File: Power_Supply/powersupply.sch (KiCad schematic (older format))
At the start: 80 parts, among them J1 1x2, J101 USB_B_Micro, J102 Conn_01x03_Male, J103 Default_Jumper, J104 Default_Jumper, J2 1x2, Q1 IRF9Z24NPBF, SW1 KMR2, SW2 joystick-K1-1506DN-01, U101 AZ1117E-3.3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

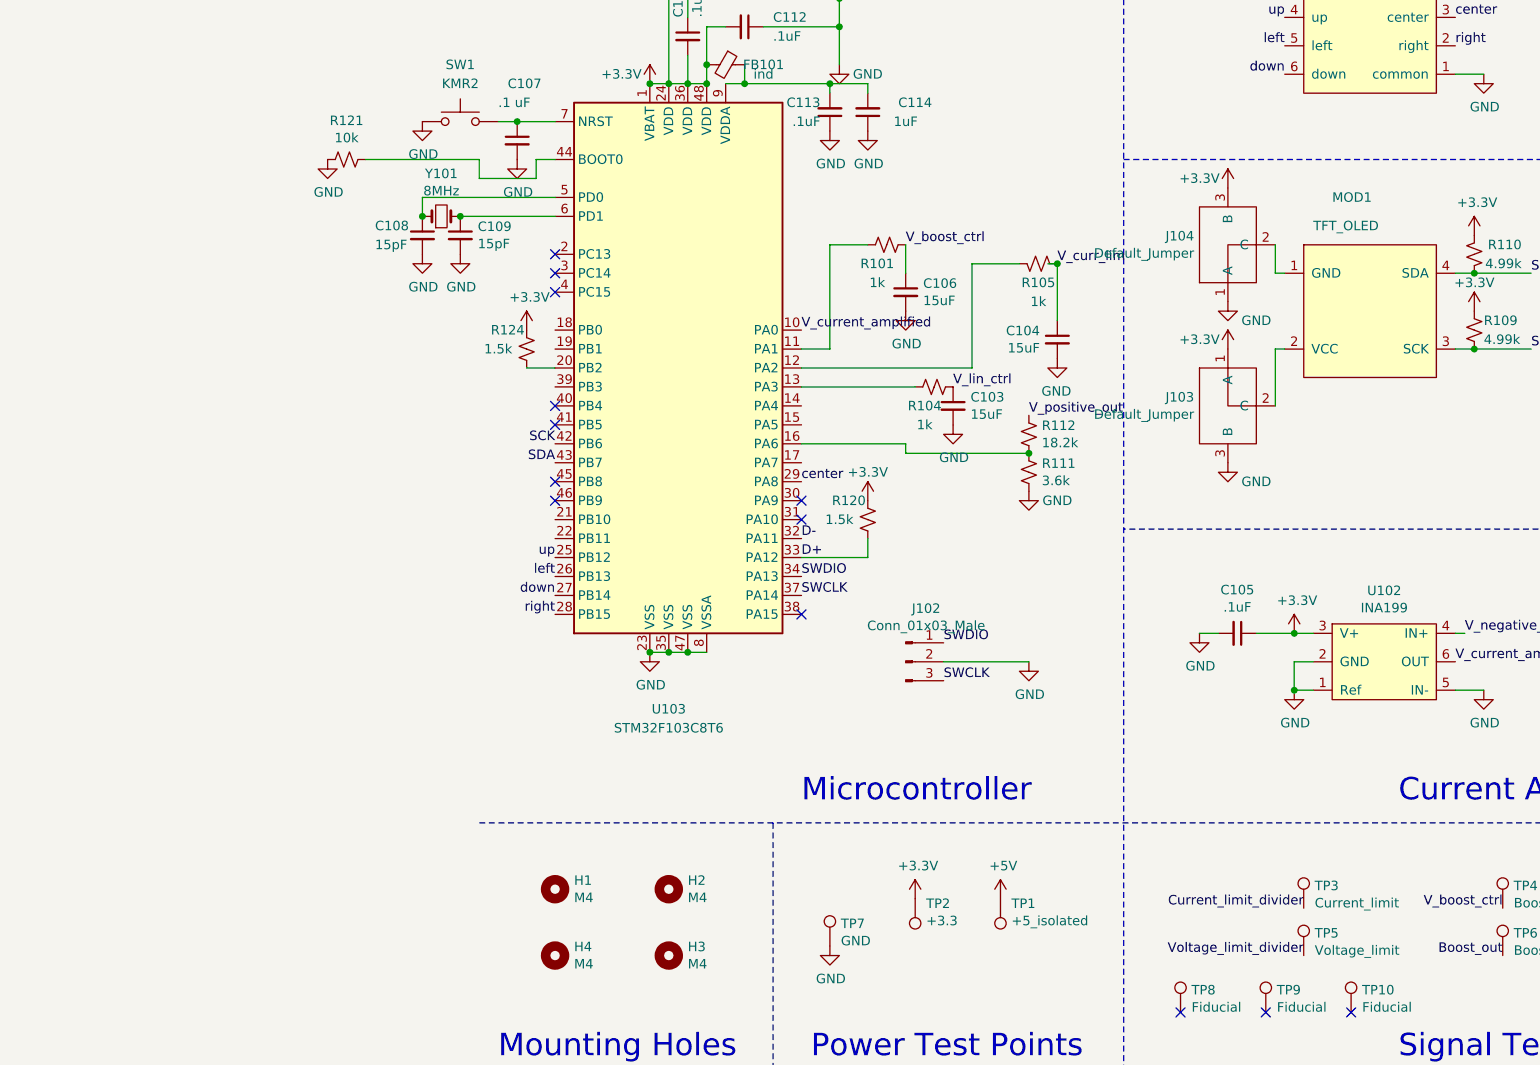
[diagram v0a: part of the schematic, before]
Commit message: Stuff for bootloader and MOSFET flat orientation
Moved power stuff to left and changed mosfet to flat orientation
Added LED for bootloader
Added button for entering bootloader mode
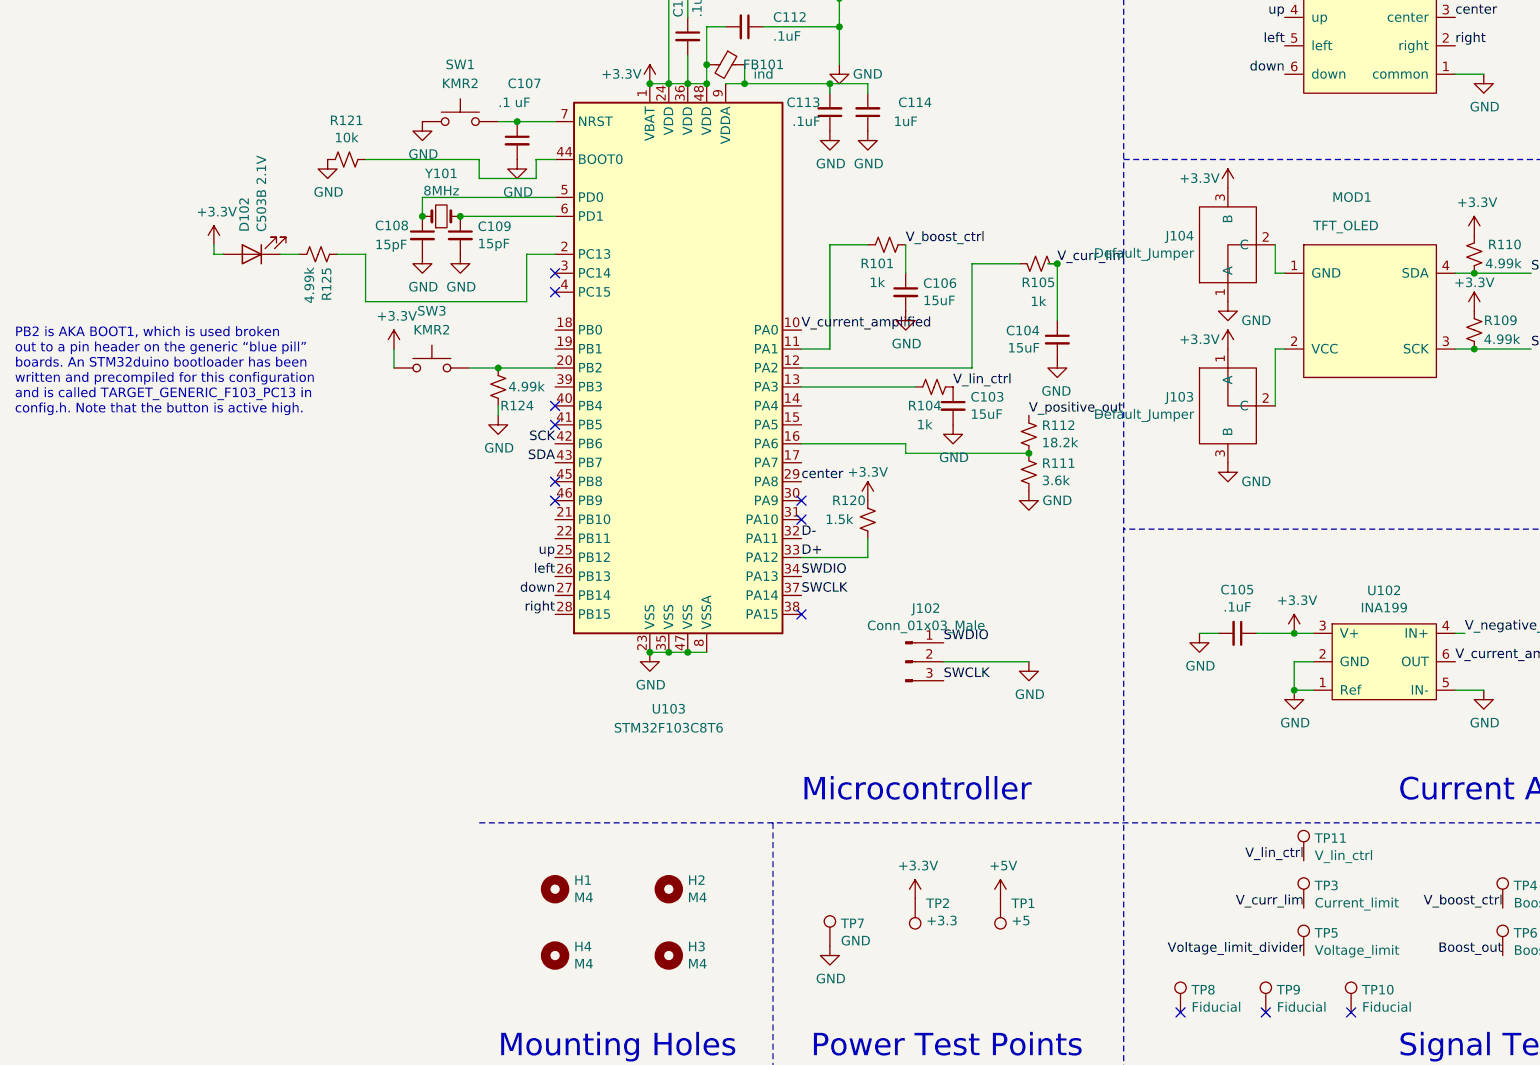
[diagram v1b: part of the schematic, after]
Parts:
- added D102: C503B 2.1V, LED_SMD:LED_0805_2012Metric, symbol Device:LED
- added R125: 4.99k, Resistor_SMD:R_0805_2012Metric, symbol Device:R_Small_US
- added SW3: KMR2, Button_Switch_SMD:SW_Push_1P1T_NO_CK_KMR2, symbol Switch:SW_Push
- added TP11: V_lin_ctrl, TestPoint:TestPoint_THTPad_1.5x1.5mm_Drill0.7mm, symbol Connector:TestPoint
- Q1: footprint powersupply:IRF9540N-PMOS -> Package_TO_SOT_THT:TO-220-3_Horizontal_TabUp
- R124: value 1.5k -> 4.99k
- TP1: value +5_isolated -> +5; footprint Connector_PinHeader_2.54mm:PinHeader_1x01_P2.54mm_Vertical -> TestPoint:TestPoint_THTPad_1.5x1.5mm_Drill0.7mm
- TP2, TP3, TP4, TP5, TP6, TP7: footprint Connector_PinHeader_2.54mm:PinHeader_1x01_P2.54mm_Vertical -> TestPoint:TestPoint_THTPad_1.5x1.5mm_Drill0.7mm
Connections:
- net +3V3: now also D102.2 (A), SW3.1; no longer R124.1
- net Current_limit_divider: no longer TP3.1
- net GND: now also R124.1
- net V_curr_lim: now also TP3.1
- net V_lin_ctrl: now also TP11.1
- net at U103.2 (PC13): now also R125.1
- net at R124.2, U103.20 (PB2): now also SW3.2
- new net: D102.1 (K), R125.2
- no-connect marks 16 -> 15
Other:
- note added: "PB2 is AKA BOOT1, which is used broken \nout to a pin header on the generic “blue pill” \nboards. An STM32duino bootloader has been \nwritten and precompiled for this configuration\nand is called TARGET_GENERIC_F103_PC13 in \nconfig.h. Note that the button is active high."
- moved on the sheet: R124
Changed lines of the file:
@@
 EESchema Schematic File Version 4
-LIBS:powersupply-cache
-EELAYER 26 0
+EELAYER 30 0
 EELAYER END
 $Descr A4 11693 8268
@@
 F 0 "Q1" H 9806 3704 50  0000 L CNN
 F 1 "IRF9Z24NPBF" H 9806 3795 50  0000 L CNN
-F 2 "powersupply:IRF9540N-PMOS" H 9800 3850 50  0001 C CNN
+F 2 "Package_TO_SOT_THT:TO-220-3_Horizontal_TabUp" H 9800 3850 50  0001 C CNN
 F 3 "~" H 9600 3750 50  0001 C CNN
 	1    9600 3750
@@
 F 0 "TP2" H 2692 6926 50  0000 R CNN
 F 1 "+3.3" H 2692 7017 50  0000 R CNN
-F 2 "Connector_PinHeader_2.54mm:PinHeader_1x01_P2.54mm_Vertical" H 2950 6900 50  0001 C CNN
+F 2 "TestPoint:TestPoint_THTPad_1.5x1.5mm_Drill0.7mm" H 2950 6900 50  0001 C CNN
 F 3 "~" H 2950 6900 50  0001 C CNN
 	1    2750 6900
@@
 P 3200 6900
 F 0 "TP1" H 3142 6926 50  0000 R CNN
-F 1 "+5_isolated" H 3142 7017 50  0000 R CNN
-F 2 "Connector_PinHeader_2.54mm:PinHeader_1x01_P2.54mm_Vertical" H 3400 6900 50  0001 C CNN
+F 1 "+5" H 3142 7017 50  0000 R CNN
+F 2 "TestPoint:TestPoint_THTPad_1.5x1.5mm_Drill0.7mm" H 3400 6900 50  0001 C CNN
 F 3 "~" H 3400 6900 50  0001 C CNN
 	1    3200 6900
@@
 F 0 "TP6" H 5908 7318 50  0000 L CNN
 F 1 "Boost_out" H 5908 7227 50  0000 L CNN
-F 2 "Connector_PinHeader_2.54mm:PinHeader_1x01_P2.54mm_Vertical" H 6050 7200 50  0001 C CNN
+F 2 "TestPoint:TestPoint_THTPad_1.5x1.5mm_Drill0.7mm" H 6050 7200 50  0001 C CNN
 F 3 "~" H 6050 7200 50  0001 C CNN
 	1    5850 7200
@@
 F 0 "TP3" H 4858 7068 50  0000 L CNN
 F 1 "Current_limit" H 4858 6977 50  0000 L CNN
-F 2 "Connector_PinHeader_2.54mm:PinHeader_1x01_P2.54mm_Vertical" H 5000 6950 50  0001 C CNN
+F 2 "TestPoint:TestPoint_THTPad_1.5x1.5mm_Drill0.7mm" H 5000 6950 50  0001 C CNN
 F 3 "~" H 5000 6950 50  0001 C CNN
 	1    4800 6950
@@
 Voltage_limit_divider
 Text Label 4800 6950 2    50   ~ 0
-Current_limit_divider
+V_curr_lim
 $Comp
 L Connector:TestPoint TP5
@@
 F 0 "TP5" H 4858 7318 50  0000 L CNN
 F 1 "Voltage_limit" H 4858 7227 50  0000 L CNN
-F 2 "Connector_PinHeader_2.54mm:PinHeader_1x01_P2.54mm_Vertical" H 5000 7200 50  0001 C CNN
+F 2 "TestPoint:TestPoint_THTPad_1.5x1.5mm_Drill0.7mm" H 5000 7200 50  0001 C CNN
 F 3 "~" H 5000 7200 50  0001 C CNN
 	1    4800 7200
@@
 F 0 "TP4" H 5908 7068 50  0000 L CNN
 F 1 "Boost_c" H 5908 6977 50  0000 L CNN
-F 2 "Connector_PinHeader_2.54mm:PinHeader_1x01_P2.54mm_Vertical" H 6050 6950 50  0001 C CNN
+F 2 "TestPoint:TestPoint_THTPad_1.5x1.5mm_Drill0.7mm" H 6050 6950 50  0001 C CNN
 F 3 "~" H 6050 6950 50  0001 C CNN
 	1    5850 6950
@@
 F 0 "TP7" H 2358 7268 50  0000 L CNN
 F 1 "GND" H 2358 7177 50  0000 L CNN
-F 2 "Connector_PinHeader_2.54mm:PinHeader_1x01_P2.54mm_Vertical" H 2500 7150 50  0001 C CNN
+F 2 "TestPoint:TestPoint_THTPad_1.5x1.5mm_Drill0.7mm" H 2500 7150 50  0001 C CNN
 F 3 "~" H 2500 7150 50  0001 C CNN
 	1    2300 7150
@@
 	1    0    0    -1
 $EndComp
-NoConn ~ 850  3500
 NoConn ~ 850  3600
 NoConn ~ 850  3700
@@
 L Device:R_Small_US R124
 U 1 1 5DC15C01
-P 700 4000
-F 0 "R124" H 600 4100 50  0000 C CNN
-F 1 "1.5k" H 550 4000 50  0000 C CNN
-F 2 "Resistor_SMD:R_0805_2012Metric" H 700 4000 50  0001 C CNN
-F 3 "~" H 700 4000 50  0001 C CNN
-	1    700  4000
-	1    0    0    -1
-$EndComp
-Wire Wire Line
-	700  4100 850  4100
+P 550 4200
+F 0 "R124" H 450 4300 50  0000 C CNN
+F 1 "4.99k" H 400 4200 50  0000 C CNN
+F 2 "Resistor_SMD:R_0805_2012Metric" H 550 4200 50  0001 C CNN
+F 3 "~" H 550 4200 50  0001 C CNN
+	1    550  4200
+	-1   0    0    1
+$EndComp
 $Comp
 L power:+3.3V #PWR0145
 U 1 1 5DC39F86
-P 700 3900
-F 0 "#PWR0145" H 700 3750 50  0001 C CNN
-F 1 "+3.3V" H 715 4073 50  0000 C CNN
-F 2 "" H 700 3900 50  0001 C CNN
-F 3 "" H 700 3900 50  0001 C CNN
-	1    700  3900
+P 0 4000
+F 0 "#PWR0145" H 0   3850 50  0001 C CNN
+F 1 "+3.3V" H 15  4173 50  0000 C CNN
+F 2 "" H 0   4000 50  0001 C CNN
+F 3 "" H 0   4000 50  0001 C CNN
+	1    0    4000
 	1    0    0    -1
 $EndComp
@@
 	1    0    0    -1
 $EndComp
+$Comp
+L Switch:SW_Push SW3
+U 1 1 5DEC94BB
+P 200 4100
+F 0 "SW3" H 200 4400 50  0000 C CNN
+F 1 "KMR2" H 200 4300 50  0000 C CNN
+F 2 "Button_Switch_SMD:SW_Push_1P1T_NO_CK_KMR2" H 200 4150 50  0001 C CNN
+F 3 "" H 200 4150 50  0001 C CNN
+	1    200  4100
+	1    0    0    -1
+$EndComp
+$Comp
+L power:GND #PWR0146
+U 1 1 5DED0756
+P 550 4350
+F 0 "#PWR0146" H 550 4100 50  0001 C CNN
+F 1 "GND" H 555 4177 50  0000 C CNN
+F 2 "" H 550 4350 50  0001 C CNN
+F 3 "" H 550 4350 50  0001 C CNN
+	1    550  4350
+	1    0    0    -1
+$EndComp
+Text Notes -2000 4350 0    50   ~ 0
+PB2 is AKA BOOT1, which is used broken \nout to a pin header on the generic “blue pill” \nboards. An STM32duino bootloader has been \nwritten and precompiled for this configuration\nand is called TARGET_GENERIC_F103_PC13 in \nconfig.h. Note that the button is active high.
+Wire Wire Line
+	400  4100 550  4100
+Connection ~ 550  4100
+Wire Wire Line
+	550  4100 850  4100
+Wire Wire Line
+	550  4300 550  4350
+Wire Wire Line
+	0    4000 0    4100
+$Comp
+L Device:R_Small_US R125
+U 1 1 5E04829A
+P -400 3500
+F 0 "R125" H -332 3546 50  0000 L CNN
+F 1 "4.99k" H -332 3455 50  0000 L CNN
+F 2 "Resistor_SMD:R_0805_2012Metric" H -400 3500 50  0001 C CNN
+F 3 "~" H -400 3500 50  0001 C CNN
+	1    -400 3500
+	0    1    1    0
+$EndComp
+$Comp
+L Device:LED D102
+U 1 1 5E0490DC
+P -750 3500
+F 0 "D102" V -711 3382 50  0000 R CNN
+F 1 "C503B 2.1V" V -802 3382 50  0000 R CNN
+F 2 "LED_SMD:LED_0805_2012Metric" H -750 3500 50  0001 C CNN
+F 3 "~" H -750 3500 50  0001 C CNN
+	1    -750 3500
+	-1   0    0    1
+$EndComp
+$Comp
+L power:+3.3V #PWR05
+U 1 1 5E049BCB
+P -950 3450
+F 0 "#PWR05" H -950 3300 50  0001 C CNN
+F 1 "+3.3V" H -935 3623 50  0000 C CNN
+F 2 "" H -950 3450 50  0001 C CNN
+F 3 "" H -950 3450 50  0001 C CNN
+	1    -950 3450
+	1    0    0    -1
+$EndComp
+Wire Wire Line
+	-950 3450 -950 3500
+Wire Wire Line
+	-950 3500 -900 3500
+Wire Wire Line
+	-600 3500 -500 3500
+Wire Wire Line
+	-300 3500 -150 3500
+Wire Wire Line
+	-150 3500 -150 3750
+Wire Wire Line
+	-150 3750 700  3750
+Wire Wire Line
+	700  3750 700  3500
+Wire Wire Line
+	700  3500 850  3500
+$Comp
+L Connector:TestPoint TP11
+U 1 1 5E0812C2
+P 4800 6700
+F 0 "TP11" H 4858 6818 50  0000 L CNN
+F 1 "V_lin_ctrl" H 4858 6727 50  0000 L CNN
+F 2 "TestPoint:TestPoint_THTPad_1.5x1.5mm_Drill0.7mm" H 5000 6700 50  0001 C CNN
+F 3 "~" H 5000 6700 50  0001 C CNN
+	1    4800 6700
+	1    0    0    -1
+$EndComp
+Text Label 4800 6700 2    50   ~ 0
+V_lin_ctrl
 $EndSCHEMATC

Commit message: updated  net name for v_positive_out_div
updated  net name for v_positive_out_div
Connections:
- net V_positive_out_div: now reaches R111.1, R112.2, U103.16 (PA6)
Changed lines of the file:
@@
 Text Label 4800 6700 2    50   ~ 0
 V_lin_ctrl
+Text Label 2200 4500 0    50   ~ 0
+V_positive_out_div
 $EndSCHEMATC

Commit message: Updated current sense amplifier part number
Didn’t include gain specifier.
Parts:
- U102: value INA199 -> INA199A1
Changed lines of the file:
@@
 U 1 1 5D4B4E12
 P 8950 4300
-F 0 "R119" V 8850 4200 50  0000 L CNN
+F 0 "R119" V 8850 4150 50  0000 L CNN
 F 1 "3k" V 8850 4400 50  0000 L CNN
 F 2 "Resistor_SMD:R_0805_2012Metric" H 8950 4300 50  0001 C CNN
@@
 P 5250 5650
 F 0 "U102" H 5225 6025 50  0000 C CNN
-F 1 "INA199" H 5225 5934 50  0000 C CNN
+F 1 "INA199A1" H 5225 5934 50  0000 C CNN
 F 2 "Package_TO_SOT_SMD:SOT-363_SC-70-6" H 5250 5950 50  0001 C CNN
 F 3 "" H 5250 5950 50  0001 C CNN
